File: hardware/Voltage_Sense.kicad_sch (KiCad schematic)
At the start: 56 parts, among them U6 TLV9002QDRQ1, U7 AMC3311QDWERQ1, U8 AMC3311QDWERQ1

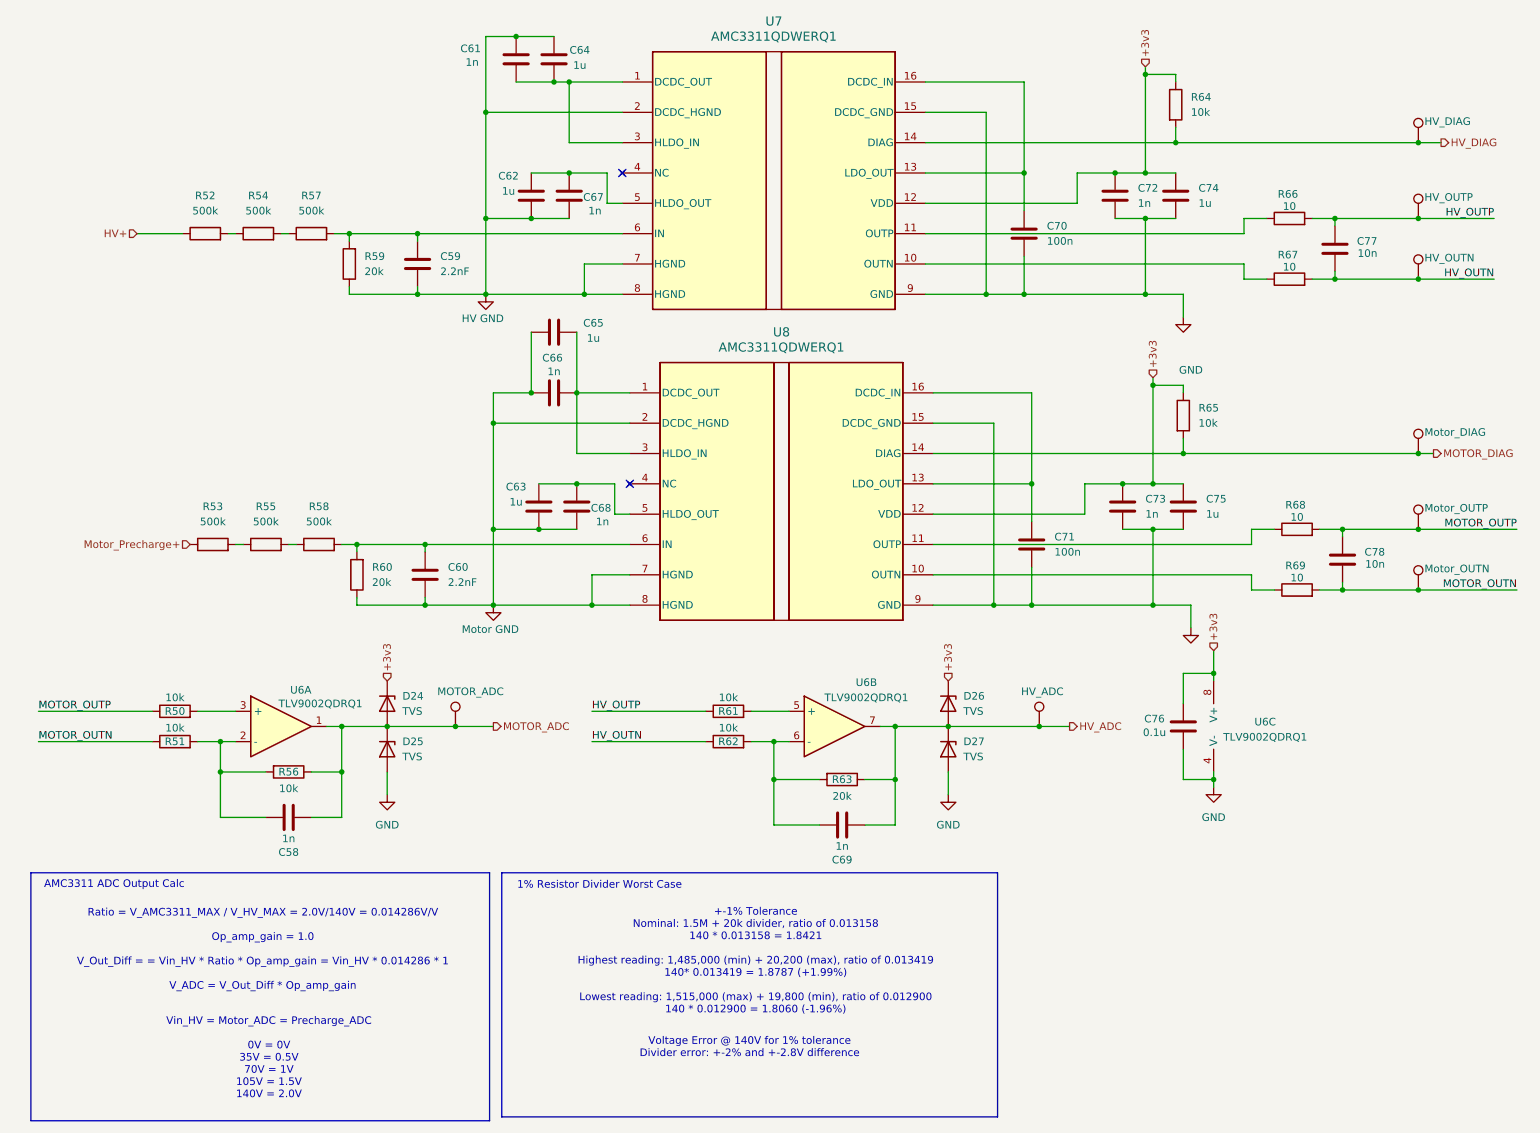
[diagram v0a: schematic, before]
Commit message: added design blocks
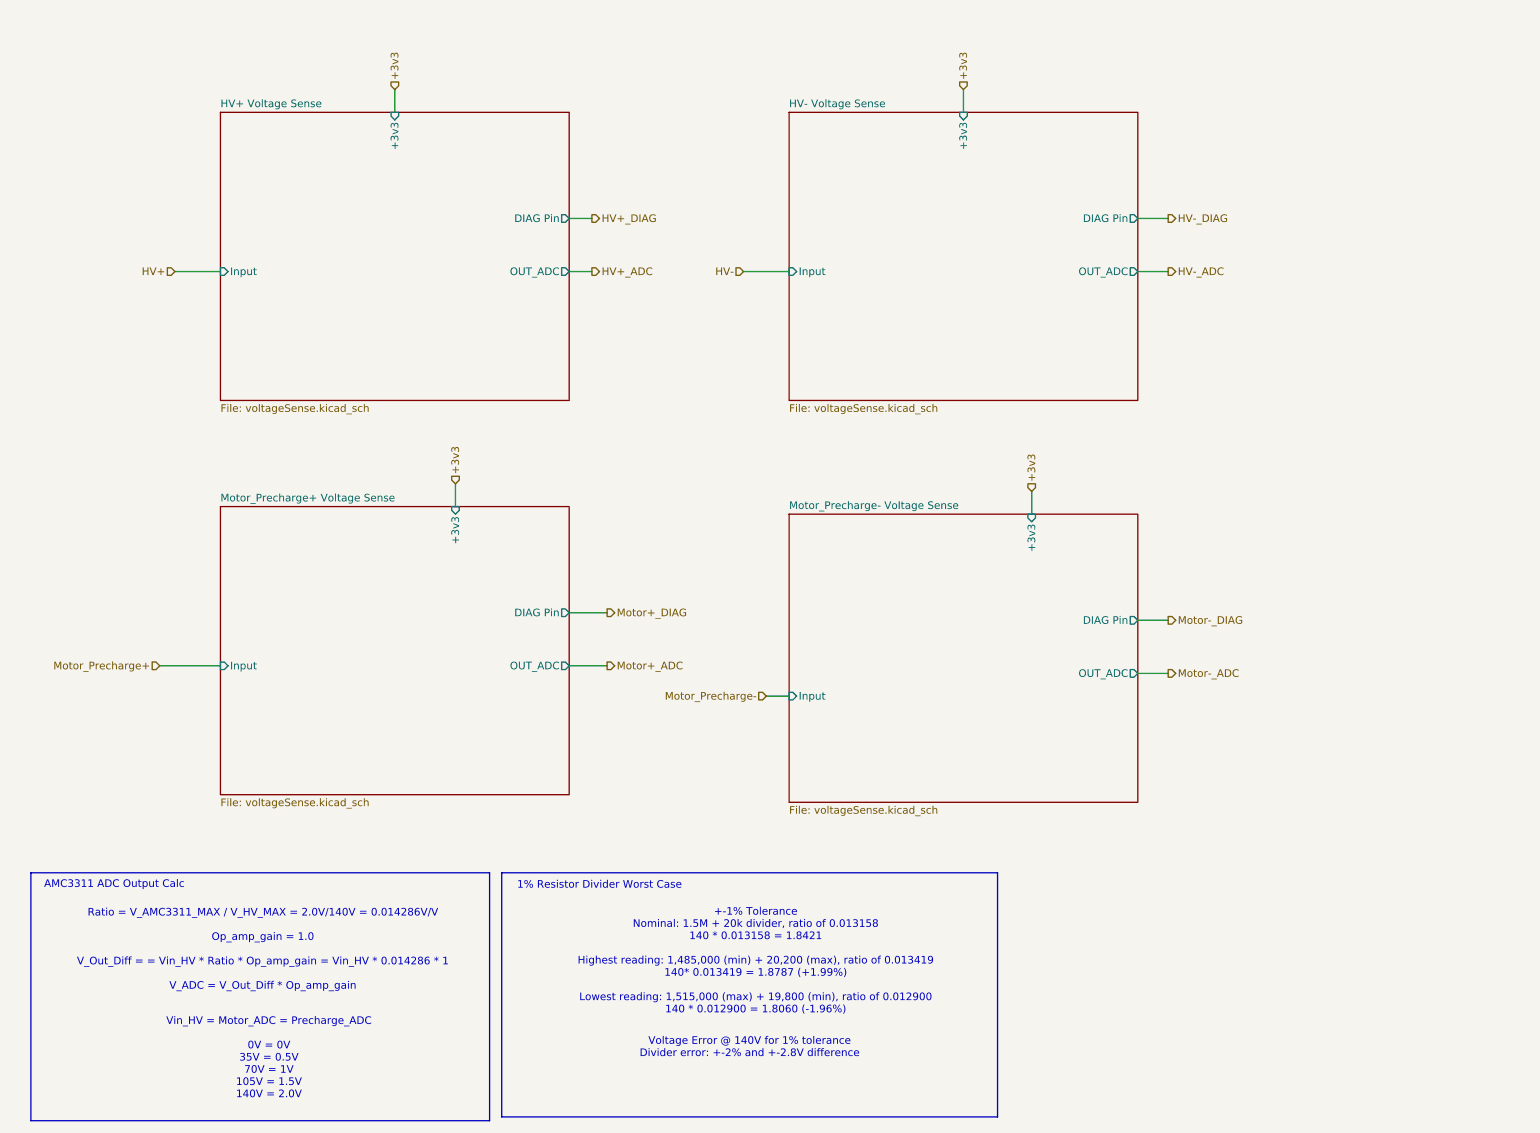
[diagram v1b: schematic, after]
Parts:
- removed C58, C61, C66, C67, C68, C69, C72, C73: 1n, symbol Device:C
- removed C59, C60: 2.2nF, symbol Device:C
- removed C62, C63, C64, C65, C74, C75: 1u, symbol Device:C
- removed C70, C71: 100n, symbol Device:C
- removed C76: 0.1u, symbol Device:C
- removed C77, C78: 10n, symbol Device:C
- removed D24, D25, D26, D27: TVS, Diode_SMD:D_SOD-123F, symbol Device:D_Zener
- removed R50, R51, R56, R61, R62, R64, R65: 10k, symbol Device:R
- removed R52, R53, R54, R55, R57, R58: 500k, symbol Device:R
- removed R59, R60, R63: 20k, symbol Device:R
- removed R66, R67, R68, R69: 10, symbol Device:R
- removed TP28: MOTOR_ADC, symbol Connector:TestPoint
- removed TP29: HV_ADC, symbol Connector:TestPoint
- removed TP30: HV_DIAG, symbol Connector:TestPoint
- removed TP31: HV_OUTP, symbol Connector:TestPoint
- removed TP32: HV_OUTN, symbol Connector:TestPoint
- removed TP33: Motor_DIAG, symbol Connector:TestPoint
- removed TP34: Motor_OUTP, symbol Connector:TestPoint
- removed TP35: Motor_OUTN, symbol Connector:TestPoint
- removed U6: TLV9002QDRQ1, Package_SO:SOIC-8_3.9x4.9mm_P1.27mm, symbol lhrs_misc:TLV9002QDRQ1
- removed U7, U8: AMC3311QDWERQ1, AMC3311QDWERQ1:DWE0016A-IPC_A, symbol AMC3311QDWERQ1:AMC3311QDWERQ1
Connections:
- no-connect marks 2 -> 0
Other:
- added sheet HV+ Voltage Sense (voltageSense.kicad_sch)
- added sheet HV- Voltage Sense (voltageSense.kicad_sch)
- added sheet Motor_Precharge+ Voltage Sense (voltageSense.kicad_sch)
- added sheet Motor_Precharge- Voltage Sense (voltageSense.kicad_sch)

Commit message: changed fully to 48 pin MCU
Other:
- sheet HV+ Voltage Sense: file voltageSense.kicad_sch -> AMC3311_Sense.kicad_sch
- sheet HV- Voltage Sense: file voltageSense.kicad_sch -> AMC3311_Sense.kicad_sch
- sheet Motor_Precharge+ Voltage Sense: file voltageSense.kicad_sch -> AMC3311_Sense.kicad_sch
- sheet Motor_Precharge- Voltage Sense: file voltageSense.kicad_sch -> AMC3311_Sense.kicad_sch
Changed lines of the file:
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@@
 		)
 	)
-	(hierarchical_label "Motor-_DIAG"
+	(hierarchical_label "MOTOR-_DIAG"
 		(shape output)
 		(at 204.47 113.03 0)
@@
 		)
 	)
-	(hierarchical_label "Motor+_ADC"
+	(hierarchical_label "MOTOR+_ADC"
 		(shape output)
 		(at 110.49 120.65 0)
@@
 		)
 	)
-	(hierarchical_label "Motor+_DIAG"
+	(hierarchical_label "MOTOR+_DIAG"
 		(shape output)
 		(at 110.49 111.76 0)
@@
 		)
 	)
-	(hierarchical_label "Motor-_ADC"
+	(hierarchical_label "MOTOR-_ADC"
 		(shape output)
 		(at 204.47 121.92 0)
@@
 			)
 		)
-		(property "Sheetfile" "voltageSense.kicad_sch"
+		(property "Sheetfile" "AMC3311_Sense.kicad_sch"
 			(at 45.72 76.7846 0)
 			(show_name no)
@@
 			)
 		)
-		(property "Sheetfile" "voltageSense.kicad_sch"
+		(property "Sheetfile" "AMC3311_Sense.kicad_sch"
 			(at 45.72 142.8246 0)
 			(show_name no)
@@
 			)
 		)
-		(property "Sheetfile" "voltageSense.kicad_sch"
+		(property "Sheetfile" "AMC3311_Sense.kicad_sch"
 			(at 140.97 144.0946 0)
 			(show_name no)
@@
 			)
 		)
-		(property "Sheetfile" "voltageSense.kicad_sch"
+		(property "Sheetfile" "AMC3311_Sense.kicad_sch"
 			(at 140.97 76.7846 0)
 			(show_name no)

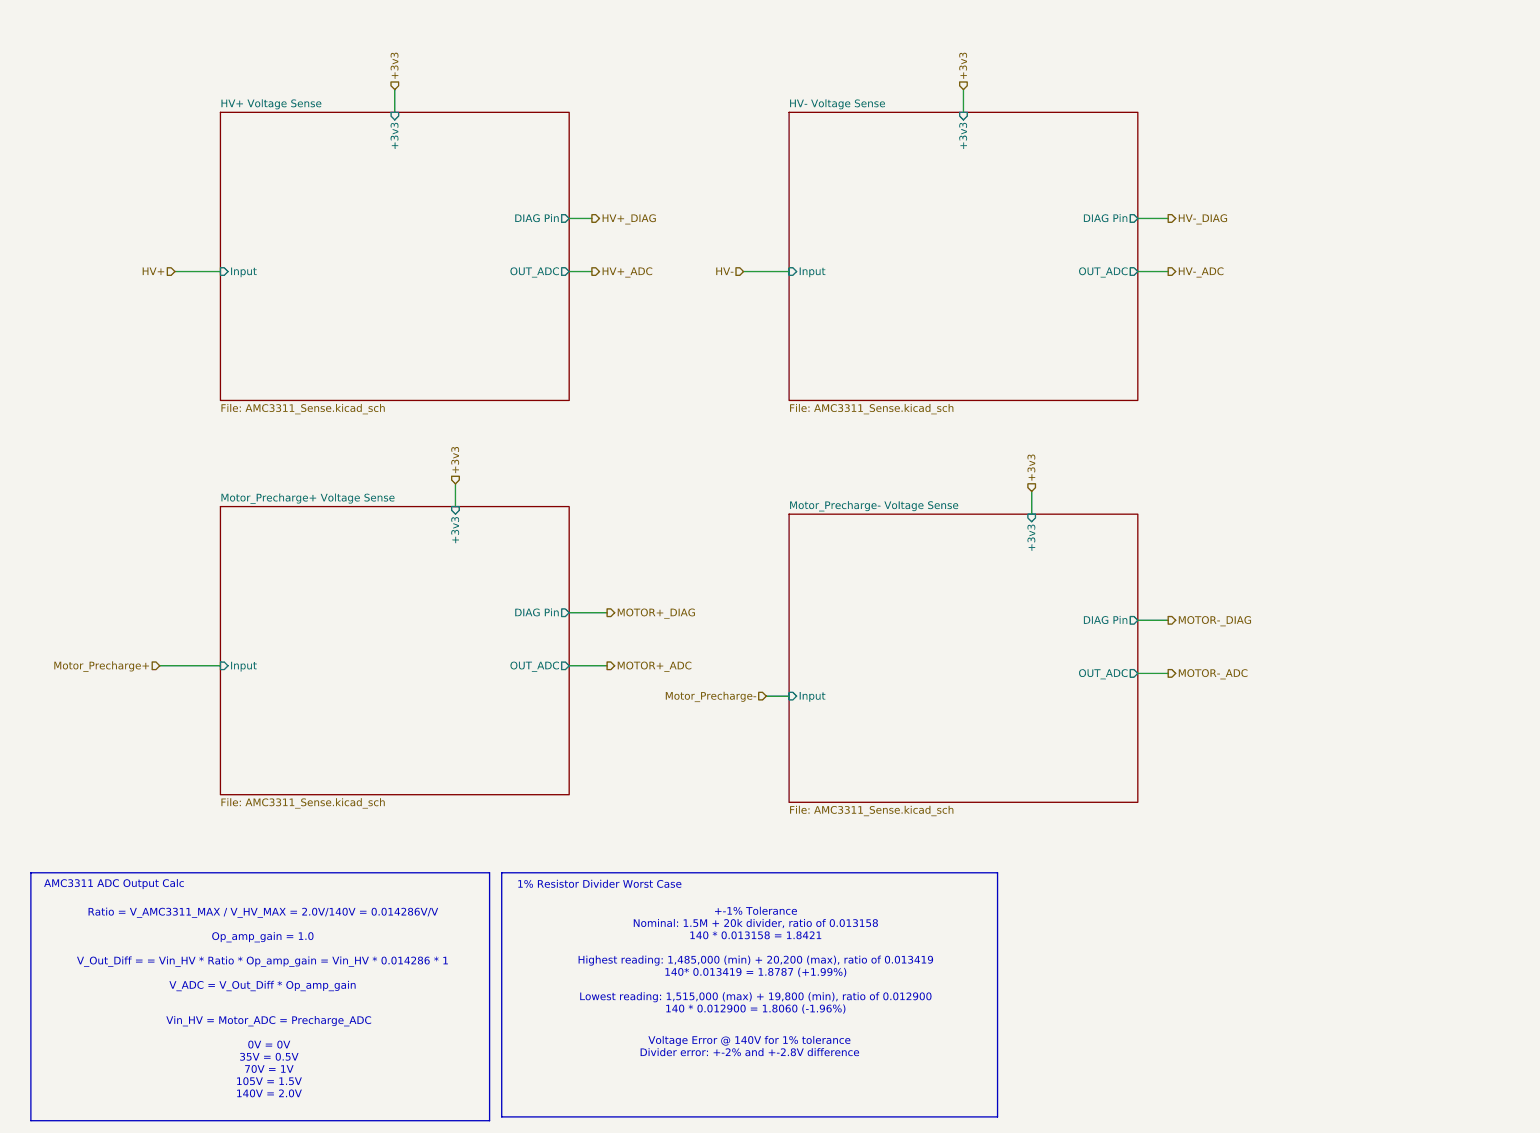
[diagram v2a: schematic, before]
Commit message: reduce op amps, better hierarchal
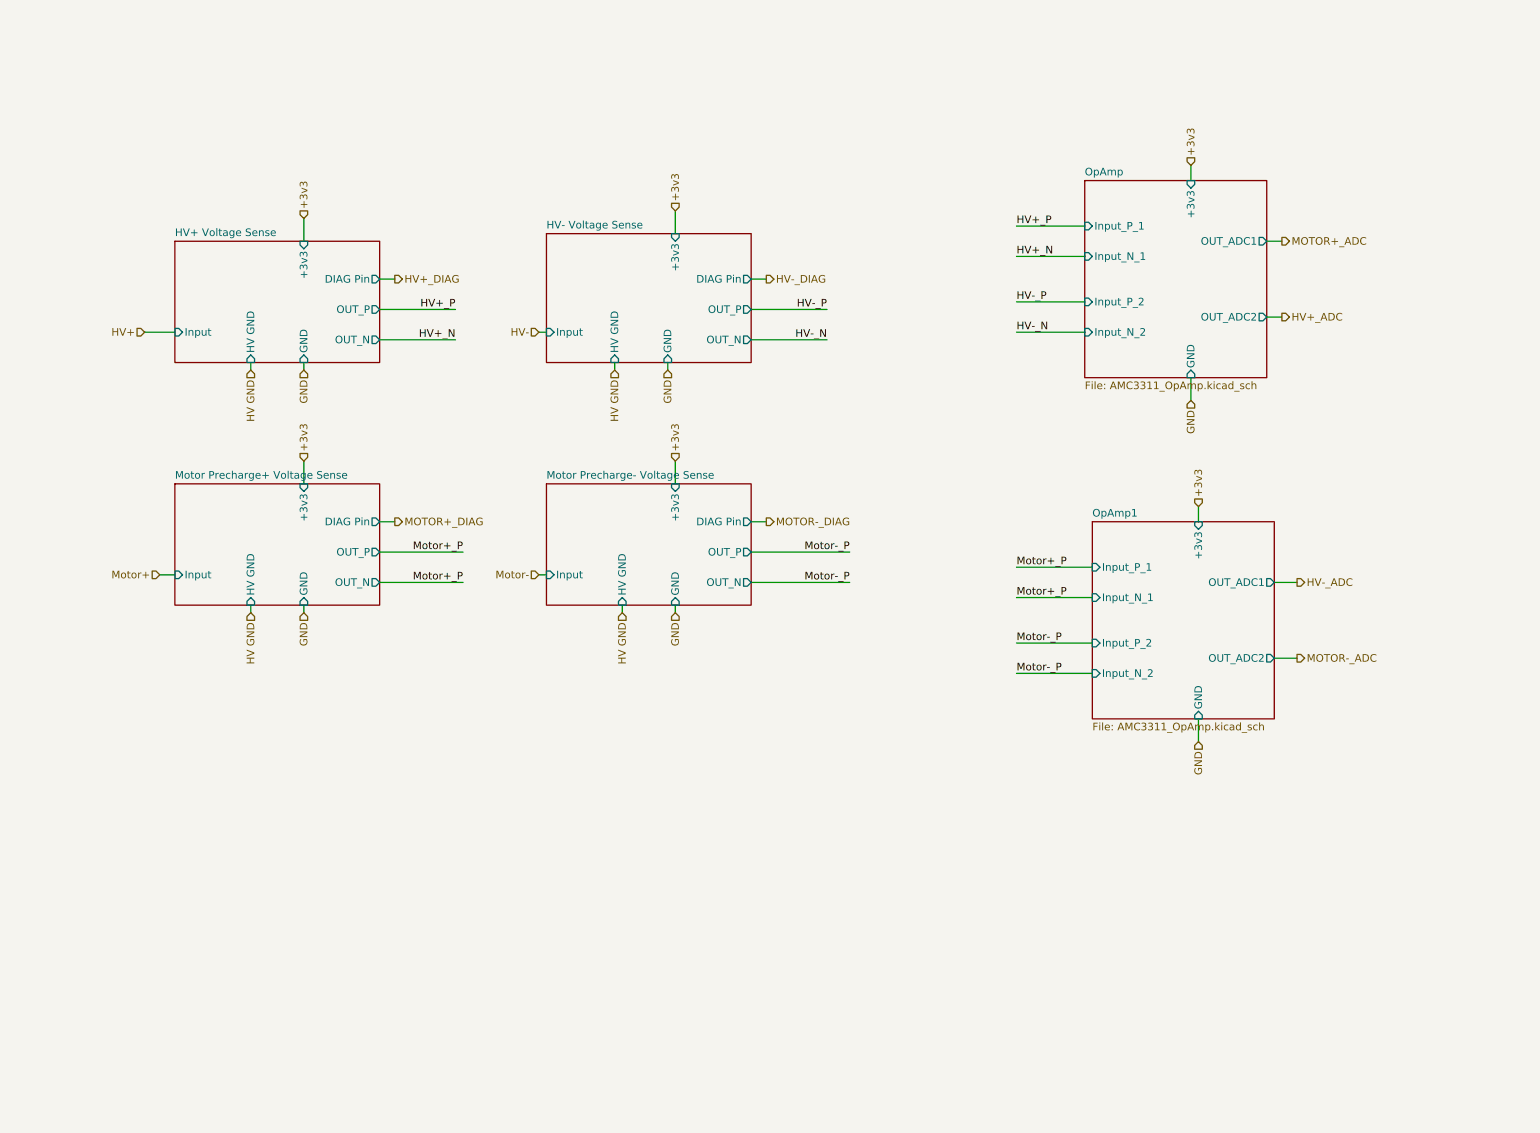
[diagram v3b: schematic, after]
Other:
- removed sheet Motor_Precharge+ Voltage Sense
- removed sheet Motor_Precharge- Voltage Sense
- added sheet Motor Precharge+ Voltage Sense (AMC3311_Sense.kicad_sch)
- added sheet Motor Precharge- Voltage Sense (AMC3311_Sense.kicad_sch)
- added sheet OpAmp (AMC3311_OpAmp.kicad_sch)
- added sheet OpAmp1 (AMC3311_OpAmp.kicad_sch)
- sheet HV+ Voltage Sense ports: added GND, HV GND, OUT_N, OUT_P; removed OUT_ADC
- sheet HV- Voltage Sense ports: added GND, HV GND, OUT_N, OUT_P; removed OUT_ADC
- note removed: "+-1% Tolerance Nominal: 1.5M + 20k divider, ratio of 0.013158 140 * 0.013158 = 1.8421 Highest reading: 1,485,000 (min) + 20,200 (max), ratio of 0.013419 140* 0.013419 = 1.8787 (+1.99%) Lowest reading: 1,515,000 (max) + 19,800 (min), ratio of 0.012900 140 * 0.012900 = 1.8060 (-1.96%)"
- note removed: "1% Resistor Divider Worst Case"
- note removed: "AMC3311 ADC Output Calc"
- note removed: "Ratio = V_AMC3311_MAX / V_HV_MAX = 2.0V/140V = 0.014286V/V Op_amp_gain = 1.0 V_Out_Diff = = Vin_HV * Ratio * Op_amp_gain = Vin_HV * 0.014286 * 1 V_ADC = V_Out_Diff * Op_amp_gain"
- note removed: "Vin_HV = Motor_ADC = Precharge_ADC 0V = 0V 35V = 0.5V 70V = 1V 105V = 1.5V 140V = 2.0V"
- note removed: "Voltage Error @ 140V for 1% tolerance Divider error: +-2% and +-2.8V difference"
